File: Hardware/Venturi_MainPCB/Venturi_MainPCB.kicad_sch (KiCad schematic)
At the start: 72 parts, among them J1 Battery, J2 ESC_PWM, J3 ESC_P, J4 ESC_N, J5 M1, J6 M1, J7 Sensor-PCB, Q1 BSS138, Q2 DMP3013SFV, SW1 POWER_EN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

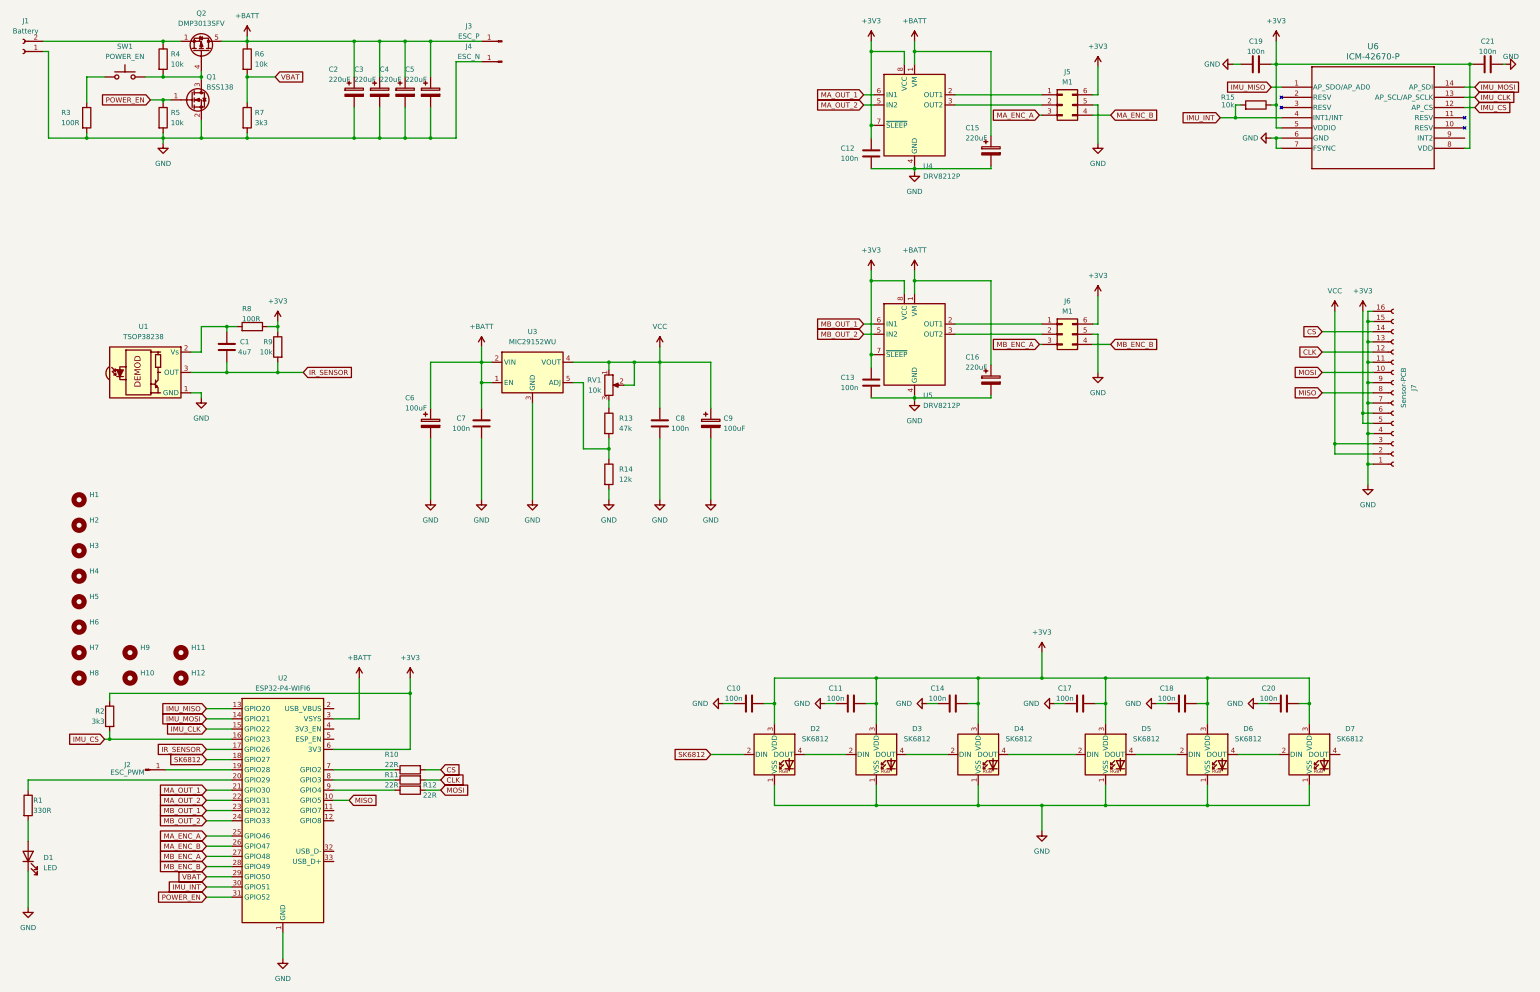
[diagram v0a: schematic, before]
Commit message: Switched to pure ESP-IDF for the ESP32-P4. Added custom firmware for the onboard ESP32-C6
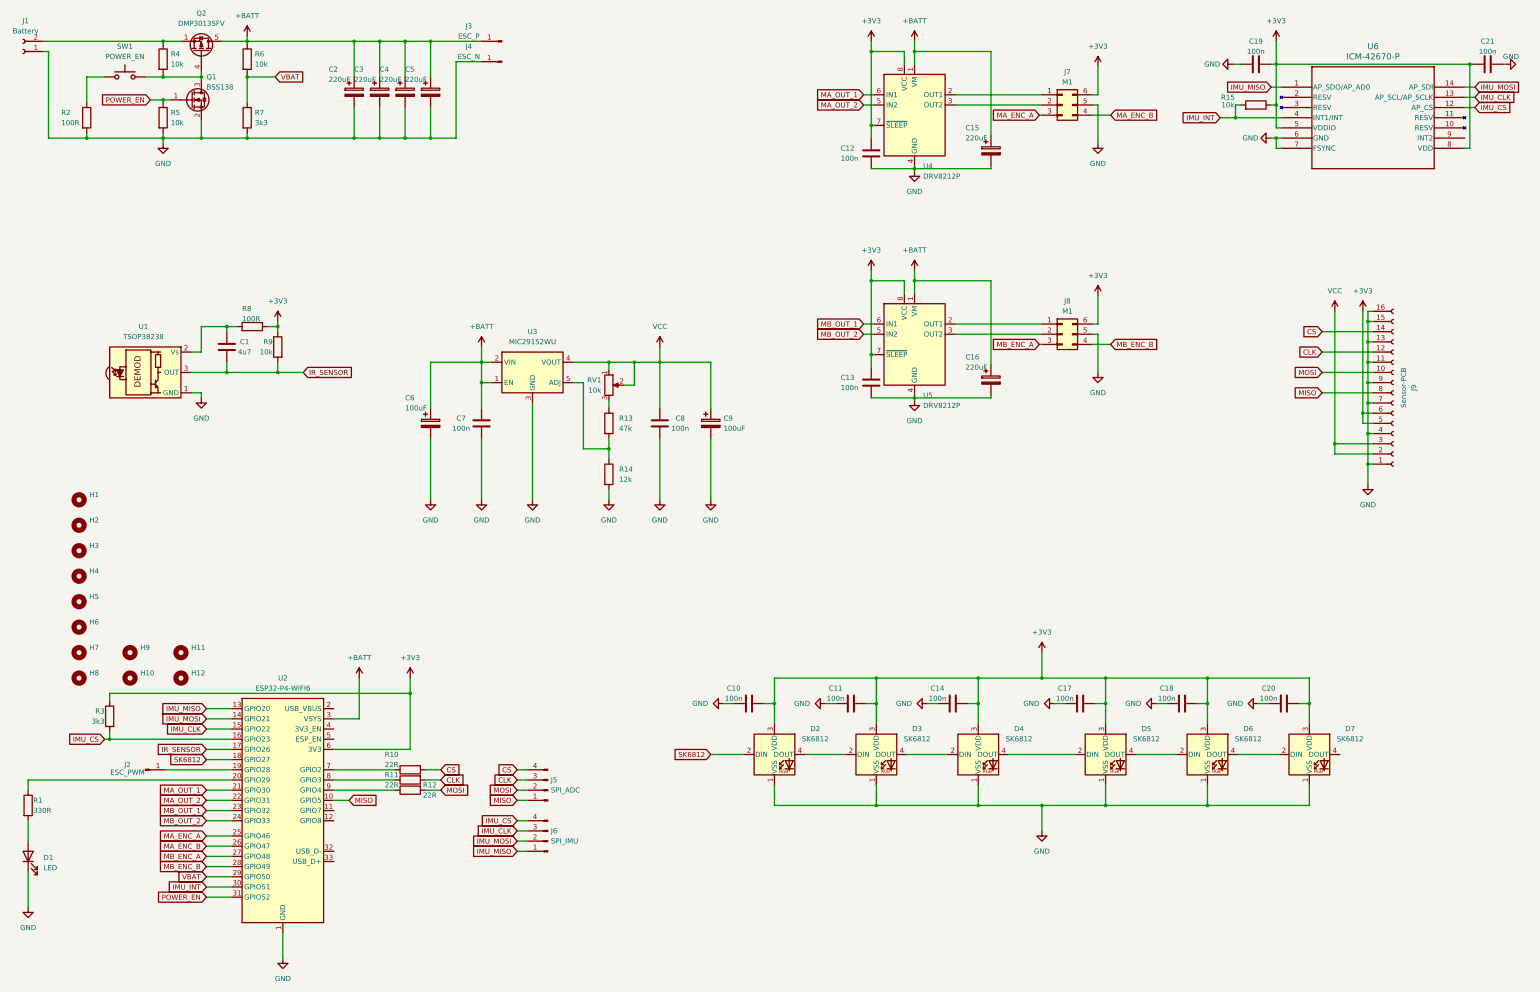
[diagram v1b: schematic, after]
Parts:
- added J5: SPI_ADC, Connector_PinHeader_1.27mm:PinHeader_1x04_P1.27mm_Vertical_SMD_Pin1Left, symbol Connector:Conn_01x04_Pin
- added J6: SPI_IMU, Connector_PinHeader_1.27mm:PinHeader_1x04_P1.27mm_Vertical_SMD_Pin1Left, symbol Connector:Conn_01x04_Pin
- renumbered J5 to J7, J6 to J8, J7 to J9, R3 to R2, R2 to R3
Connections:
- net CLK: now also J5.3 (Pin_3)
- net CS: now also J5.4 (Pin_4)
- net IMU_CLK: now also J6.3 (Pin_3)
- net IMU_CS: now also J6.4 (Pin_4)
- net IMU_MISO: now also J6.1 (Pin_1)
- net IMU_MOSI: now also J6.2 (Pin_2)
- net MISO: now also J5.1 (Pin_1)
- net MOSI: now also J5.2 (Pin_2)
